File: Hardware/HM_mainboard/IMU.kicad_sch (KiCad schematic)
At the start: 12 parts, among them U5 MC6470, U6 BNO055

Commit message: Updated BOM
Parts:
- C15, C16, C17, C18, C20: Digikey 1276-CL10B104KB8NNNLCT -> 1276-CL10B104KB8NNNLCT-ND
- C19: Mouser 647-F921E105KPA -> F921E105KPA
- R11: value 10k/1% -> 10k; Mouser 660-RN73H1JT1002F100 -> (none)
- U5: Mouser 498-MC6470 -> MC6470
- U6: Mouser 262-BNO055 -> (none)
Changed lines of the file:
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@@
       (effects (font (size 1.27 1.27)) hide)
     )
-    (property "Mouser" "647-F921E105KPA" (at 172.085 77.47 0)
+    (property "Mouser" "F921E105KPA" (at 172.085 77.47 0)
       (effects (font (size 1.27 1.27)) hide)
     )
@@
       (effects (font (size 1.778 1.778)) (justify bottom))
     )
-    (property "Value" "10k/1%" (at 155.575 70.485 0)
+    (property "Value" "10k" (at 155.575 70.485 0)
       (effects (font (size 1.778 1.778)) (justify top))
     )
@@
     )
     (property "Reichelt" "" (at 155.575 64.77 0)
-      (effects (font (size 1.27 1.27)) hide)
-    )
-    (property "Mouser" "660-RN73H1JT1002F100" (at 155.575 64.77 0)
       (effects (font (size 1.27 1.27)) hide)
     )
@@
       (effects (font (size 1.27 1.27)) hide)
     )
-    (property "Digikey" "1276-CL10B104KB8NNNLCT" (at 252.095 52.705 0)
+    (property "Digikey" "1276-CL10B104KB8NNNLCT-ND" (at 252.095 52.705 0)
       (effects (font (size 1.27 1.27)) hide)
     )
@@
       (effects (font (size 1.27 1.27)) hide)
     )
-    (property "Digikey" "1276-CL10B104KB8NNNLCT" (at 56.515 102.235 0)
+    (property "Digikey" "1276-CL10B104KB8NNNLCT-ND" (at 56.515 102.235 0)
       (effects (font (size 1.27 1.27)) hide)
     )
@@
       (effects (font (size 1.27 1.27)) (justify bottom) hide)
     )
-    (property "Mouser" "498-MC6470" (at 60.96 158.115 0)
+    (property "Mouser" "MC6470" (at 60.96 158.115 0)
       (effects (font (size 1.27 1.27)) hide)
     )
@@
       (effects (font (size 1.27 1.27)) hide)
     )
-    (property "Digikey" "1276-CL10B104KB8NNNLCT" (at 86.995 78.105 0)
+    (property "Digikey" "1276-CL10B104KB8NNNLCT-ND" (at 86.995 78.105 0)
       (effects (font (size 1.27 1.27)) hide)
     )
@@
       (effects (font (size 1.27 1.27)) hide)
     )
-    (property "Digikey" "1276-CL10B104KB8NNNLCT" (at 102.87 151.13 0)
+    (property "Digikey" "1276-CL10B104KB8NNNLCT-ND" (at 102.87 151.13 0)
       (effects (font (size 1.27 1.27)) hide)
     )
@@
     )
     (property "Reichelt" "" (at 178.435 57.15 0)
-      (effects (font (size 1.27 1.27)) hide)
-    )
-    (property "Mouser" "262-BNO055" (at 178.435 57.15 0)
       (effects (font (size 1.27 1.27)) hide)
     )
@@
       (effects (font (size 1.778 1.778)) (justify bottom))
     )
-    (property "Value" "10k/1%" (at 87.63 156.21 0)
+    (property "Value" "10k" (at 87.63 156.21 0)
       (effects (font (size 1.778 1.778)) (justify top))
     )
@@
     )
     (property "Reichelt" "" (at 87.63 153.035 0)
-      (effects (font (size 1.27 1.27)) hide)
-    )
-    (property "Mouser" "660-RN73H1JT1002F100" (at 87.63 153.035 0)
       (effects (font (size 1.27 1.27)) hide)
     )
@@
       (effects (font (size 1.27 1.27)) hide)
     )
-    (property "Digikey" "1276-CL10B104KB8NNNLCT" (at 158.115 50.8 0)
+    (property "Digikey" "1276-CL10B104KB8NNNLCT-ND" (at 158.115 50.8 0)
       (effects (font (size 1.27 1.27)) hide)
     )
@@
       (effects (font (size 1.778 1.778)) (justify bottom))
     )
-    (property "Value" "10k/1%" (at 155.575 88.265 0)
+    (property "Value" "10k" (at 155.575 88.265 0)
       (effects (font (size 1.778 1.778)) (justify top))
     )
@@
       (effects (font (size 1.27 1.27)) hide)
     )
-    (property "Mouser" "660-RN73H1JT1002F100" (at 155.575 82.55 0)
-      (effects (font (size 1.27 1.27)) hide)
-    )

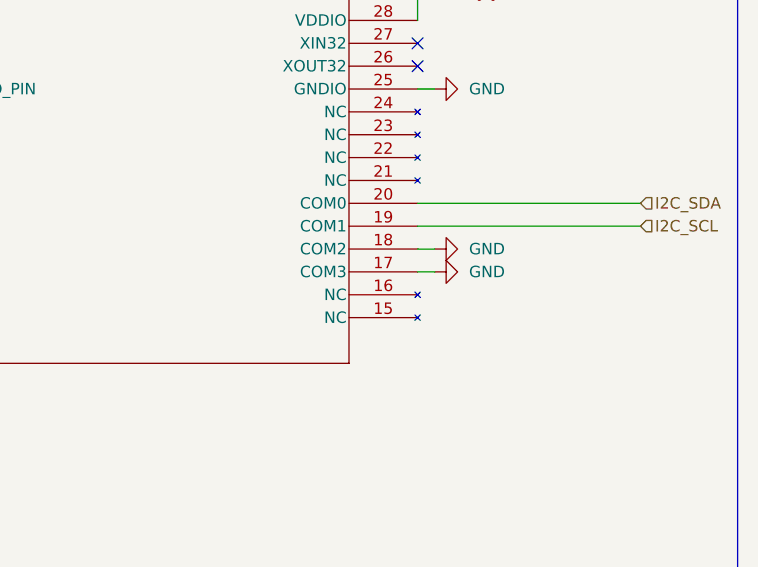
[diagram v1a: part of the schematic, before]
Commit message: Fixed missing GND connections of BNO055 at Pin 15 and 16
Bugfix due to wrong pin assignments in symbol library
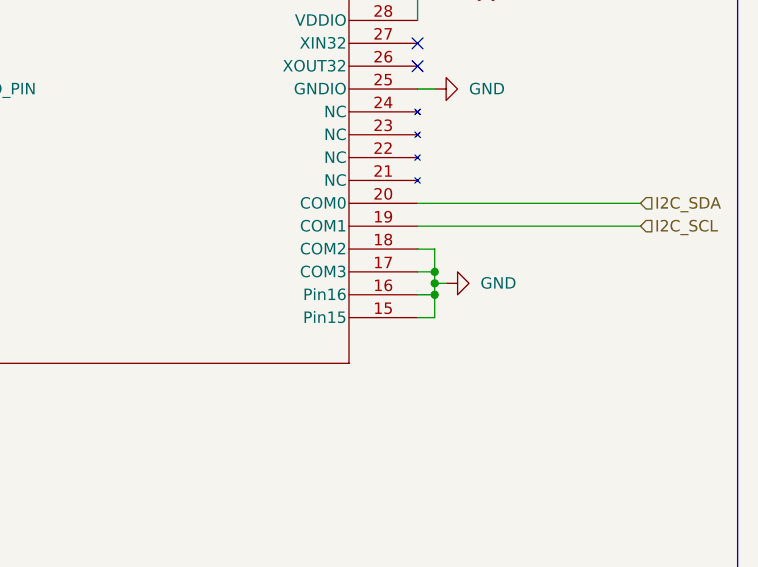
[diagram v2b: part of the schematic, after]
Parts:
- U6: footprint HeadMouse:QFN_BNO055_BOS -> QFN_BNO055_BOS
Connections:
- net GND: now also U6.15 (Pin15), U6.16 (Pin16)
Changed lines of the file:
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@@
   (junction (at 84.455 145.415) (diameter 0) (color 0 0 0 0)
   )
+  (junction (at 246.38 85.09) (diameter 0) (color 0 0 0 0)
+  )
+  (junction (at 246.38 86.36) (diameter 0) (color 0 0 0 0)
+  )
   (junction (at 158.115 45.72) (diameter 0) (color 0 0 0 0)
+  )
+  (junction (at 246.38 87.63) (diameter 0) (color 0 0 0 0)
   )
   (junction (at 86.995 73.025) (diameter 0) (color 0 0 0 0)
@@
     (stroke (width 0) (type default))
   )
+  (wire (pts (xy 244.475 90.17) (xy 246.38 90.17))
+    (stroke (width 0) (type default))
+  )
   (wire (pts (xy 41.275 70.485) (xy 46.355 70.485))
     (stroke (width 0) (type default))
@@
     (stroke (width 0) (type default))
   )
+  (wire (pts (xy 244.475 87.63) (xy 246.38 87.63))
+    (stroke (width 0) (type default))
+  )
   (wire (pts (xy 244.475 82.55) (xy 246.38 82.55))
     (stroke (width 0) (type default))
@@
     (stroke (width 0) (type default))
   )
+  (wire (pts (xy 246.38 87.63) (xy 246.38 86.36))
+    (stroke (width 0) (type default))
+  )
   (wire (pts (xy 175.895 68.58) (xy 177.165 68.58))
     (stroke (width 0) (type default))
@@
     (stroke (width 0) (type default))
   )
+  (wire (pts (xy 246.38 86.36) (xy 246.38 85.09))
+    (stroke (width 0) (type default))
+  )
   (wire (pts (xy 56.515 106.045) (xy 56.515 107.315))
     (stroke (width 0) (type default))
@@
     (stroke (width 0) (type default))
   )
+  (wire (pts (xy 246.38 82.55) (xy 246.38 85.09))
+    (stroke (width 0) (type default))
+  )
   (wire (pts (xy 149.225 64.77) (xy 150.495 64.77))
     (stroke (width 0) (type default))
@@
     (stroke (width 0) (type default))
   )
+  (wire (pts (xy 246.38 90.17) (xy 246.38 87.63))
+    (stroke (width 0) (type default))
+  )
   (wire (pts (xy 86.995 73.025) (xy 86.995 71.755))
     (stroke (width 0) (type default))
@@
   )
   (wire (pts (xy 84.455 145.415) (xy 78.74 145.415))
+    (stroke (width 0) (type default))
+  )
+  (wire (pts (xy 247.65 86.36) (xy 246.38 86.36))
     (stroke (width 0) (type default))
   )
@@
       (effects (font (size 1.524 1.524)))
     )
-    (property "Footprint" "HeadMouse:QFN_BNO055_BOS" (at 178.435 57.15 0)
+    (property "Footprint" "QFN_BNO055_BOS" (at 178.435 57.15 0)
       (effects (font (size 1.27 1.27) italic) hide)
     )
-    (property "Datasheet" "https://www.bosch-sensortec.com/media/boschsensortec/downloads/datasheets/bst-bno055-ds000.pdf" (at 178.435 57.15 0)
+    (property "Datasheet" "BNO055" (at 178.435 57.15 0)
       (effects (font (size 1.27 1.27) italic) hide)
     )
@@
     (pin "13")
     (pin "14")
-    (pin "15")
-    (pin "16")
     (pin "17")
     (pin "18")
@@
     (pin "23")
     (pin "24")
-    (pin "25")
     (pin "26")
     (pin "27")
@@
     (pin "8")
     (pin "9")
+    (pin "15")
+    (pin "16")
+    (pin "25")
     (instances
       (project "HM_mainboard"
@@
     )
   )
-  (symbol (lib_name "GND_1") (lib_id "power:GND") (at 246.38 85.09 90) (unit 1)
-    (in_bom yes) (on_board yes) (dnp no) (fields_autoplaced)
-    (property "Reference" "#PWR06" (at 252.73 85.09 0)
-      (effects (font (size 1.27 1.27)) hide)
-    )
-    (property "Value" "GND" (at 250.19 85.09 90)
+  (symbol (lib_name "GND_1") (lib_id "power:GND") (at 247.65 86.36 90) (unit 1)
+    (in_bom yes) (on_board yes) (dnp no) (fields_autoplaced)
+    (property "Reference" "#PWR06" (at 254 86.36 0)
+      (effects (font (size 1.27 1.27)) hide)
+    )
+    (property "Value" "GND" (at 251.46 86.36 90)
       (effects (font (size 1.27 1.27)) (justify right))
     )
-    (property "Footprint" "" (at 246.38 85.09 0)
-      (effects (font (size 1.27 1.27)) hide)
-    )
-    (property "Datasheet" "" (at 246.38 85.09 0)
+    (property "Footprint" "" (at 247.65 86.36 0)
+      (effects (font (size 1.27 1.27)) hide)
+    )
+    (property "Datasheet" "" (at 247.65 86.36 0)
       (effects (font (size 1.27 1.27)) hide)
     )
@@
         )
       )
-    )
-  )
-  (symbol (lib_name "GND_1") (lib_id "power:GND") (at 246.38 82.55 90) (unit 1)
-    (in_bom yes) (on_board yes) (dnp no) (fields_autoplaced)
-    (property "Reference" "#PWR06" (at 252.73 82.55 0)
-      (effects (font (size 1.27 1.27)) hide)
-    )
-    (property "Value" "GND" (at 250.19 82.55 90)
-      (effects (font (size 1.27 1.27)) (justify right))
-    )
-    (property "Footprint" "" (at 246.38 82.55 0)
-      (effects (font (size 1.27 1.27)) hide)
-    )
-    (property "Datasheet" "" (at 246.38 82.55 0)
-      (effects (font (size 1.27 1.27)) hide)
-    )
-    (pin "1")
-    (instances
-      (project "HM_mainboard"
-        (path "/54a6df43-5475-46a2-9916-8b0260700d4c"
-          (reference "#PWR06") (unit 1)
-        )
-        (path "/54a6df43-5475-46a2-9916-8b0260700d4c/8a725ce3-408a-4762-9df2-b56094186e56"
-          (reference "#PWR09") (unit 1)
-        )
-        (path "/54a6df43-5475-46a2-9916-8b0260700d4c/9043a365-e24a-41b8-9f6d-decb4da0da6a"
-          (reference "#PWR047") (unit 1)
-        )
-      )

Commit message: Added testpoints to pcb
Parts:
- added TP7: TestPoint_2Pole, Connector_PinHeader_2.54mm:PinHeader_1x02_P2.54mm_Vertical, symbol Connector:TestPoint_2Pole
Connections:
- net I2C_SCL: now also TP7.1
- net I2C_SDA: now also TP7.2
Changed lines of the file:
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@@
     (title "Intertia_Measurement_Unit")
   )
+  (junction (at 255.905 80.01) (diameter 0) (color 0 0 0 0)
+  )
   (junction (at 56.515 97.155) (diameter 0) (color 0 0 0 0)
+  )
+  (junction (at 266.065 77.47) (diameter 0) (color 0 0 0 0)
   )
   (junction (at 41.275 67.945) (diameter 0) (color 0 0 0 0)
@@
     (stroke (width 0) (type default))
   )
+  (wire (pts (xy 255.905 74.295) (xy 255.905 80.01))
+    (stroke (width 0) (type default))
+  )
   (wire (pts (xy 177.165 68.58) (xy 177.165 67.31))
     (stroke (width 0) (type default))
@@
     (stroke (width 0) (type default))
   )
+  (wire (pts (xy 266.065 77.47) (xy 269.24 77.47))
+    (stroke (width 0) (type default))
+  )
   (wire (pts (xy 65.405 92.075) (xy 65.405 94.615))
     (stroke (width 0) (type default))
@@
     (stroke (width 0) (type default))
   )
+  (wire (pts (xy 266.065 74.295) (xy 266.065 77.47))
+    (stroke (width 0) (type default))
+  )
   (wire (pts (xy 174.625 90.17) (xy 178.435 90.17))
     (stroke (width 0) (type default))
@@
     (stroke (width 0) (type default))
   )
+  (wire (pts (xy 255.905 80.01) (xy 269.24 80.01))
+    (stroke (width 0) (type default))
+  )
   (wire (pts (xy 84.455 145.415) (xy 78.74 145.415))
     (stroke (width 0) (type default))
@@
     (stroke (width 0) (type default))
   )
-  (wire (pts (xy 244.475 80.01) (xy 269.24 80.01))
+  (wire (pts (xy 244.475 80.01) (xy 255.905 80.01))
     (stroke (width 0) (type default))
   )
@@
     (stroke (width 0) (type default))
   )
-  (wire (pts (xy 244.475 77.47) (xy 269.24 77.47))
+  (wire (pts (xy 244.475 77.47) (xy 266.065 77.47))
     (stroke (width 0) (type default))
   )
@@
         )
         (path "/54a6df43-5475-46a2-9916-8b0260700d4c/9043a365-e24a-41b8-9f6d-decb4da0da6a"
-          (reference "#PWR049") (unit 1)
+          (reference "#PWR048") (unit 1)
         )
       )
@@
     )
   )
+  (symbol (lib_id "Connector:TestPoint_2Pole") (at 260.985 74.295 0) (unit 1)
+    (in_bom yes) (on_board yes) (dnp no) (fields_autoplaced)
+    (property "Reference" "TP7" (at 260.985 71.12 0)
+      (effects (font (size 1.27 1.27)))
+    )
+    (property "Value" "TestPoint_2Pole" (at 260.985 71.12 0)
+      (effects (font (size 1.27 1.27)) hide)
+    )
+    (property "Footprint" "Connector_PinHeader_2.54mm:PinHeader_1x02_P2.54mm_Vertical" (at 260.985 74.295 0)
+      (effects (font (size 1.27 1.27)) hide)
+    )
+    (property "Datasheet" "~" (at 260.985 74.295 0)
+      (effects (font (size 1.27 1.27)) hide)
+    )
+    (pin "1")
+    (pin "2")
+    (instances
+      (project "HM_mainboard"
+        (path "/54a6df43-5475-46a2-9916-8b0260700d4c/9043a365-e24a-41b8-9f6d-decb4da0da6a"
+          (reference "TP7") (unit 1)
+        )
+      )
+    )
+  )
   (symbol (lib_name "GND_1") (lib_id "power:GND") (at 65.405 94.615 0) (unit 1)
     (in_bom yes) (on_board yes) (dnp no) (fields_autoplaced)
@@
         )
         (path "/54a6df43-5475-46a2-9916-8b0260700d4c/9043a365-e24a-41b8-9f6d-decb4da0da6a"
-          (reference "#PWR048") (unit 1)
-        )
-      )
+          (reference "#PWR047") (unit 1)
+        )
+      )

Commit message: Updated schematic and PCB according to Email from BA on 16th of April
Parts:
- C19: value 1.0uF-25V-(+80/-20%) -> 1.0uF
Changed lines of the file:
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@@
-    (stroke (width 0) (type default))
-  )
-  (wire (pts (xy 78.74 155.575) (xy 78.74 158.115))
     (stroke (width 0) (type default))
   )
@@
     (stroke (width 0) (type default))
   )
-  (wire (pts (xy 81.915 158.115) (xy 78.74 158.115))
+  (wire (pts (xy 82.55 155.575) (xy 78.74 155.575))
     (stroke (width 0) (type default))
   )
@@
     (stroke (width 0) (type default))
   )
-  (rectangle (start 133.985 16.51) (end 280.035 139.7)
+  (rectangle (start 133.985 16.51) (end 280.035 114.3)
     (stroke (width 0) (type default))
     (fill (type none))
@@
     (effects (font (size 1.27 1.27)) (justify right))
   )
-  (hierarchical_label "MC6470_INT" (shape input) (at 81.915 158.115 0) (fields_autoplaced)
+  (hierarchical_label "MC6470_INT" (shape input) (at 82.55 155.575 0) (fields_autoplaced)
     (effects (font (size 1.27 1.27)) (justify left))
   )
@@
       (effects (font (size 1.27 1.27)))
     )
-    (property "Value" "1.0uF-25V-(+80/-20%)" (at 172.085 73.66 90)
+    (property "Value" "1.0uF" (at 172.085 73.66 90)
       (effects (font (size 1.27 1.27)))
     )
@@
   (symbol (lib_id "esp32-thing-eagle-import:10KOHM-1/10W-1%(0603)0603") (at 87.63 153.035 180) (unit 1)
     (in_bom yes) (on_board yes) (dnp no)
-    (property "Reference" "R11" (at 87.63 149.86 0)
+    (property "Reference" "R11" (at 87.63 147.32 0)
       (effects (font (size 1.778 1.778)) (justify bottom))
     )
-    (property "Value" "10k" (at 87.63 156.21 0)
+    (property "Value" "10k" (at 87.63 151.765 0)
       (effects (font (size 1.778 1.778)) (justify top))
     )
@@
   )
   (symbol (lib_name "GND_1") (lib_id "power:GND") (at 65.405 94.615 0) (unit 1)
-    (in_bom yes) (on_board yes) (dnp no) (fields_autoplaced)
+    (in_bom yes) (on_board yes) (dnp no)
     (property "Reference" "#PWR06" (at 65.405 100.965 0)
       (effects (font (size 1.27 1.27)) hide)
     )
-    (property "Value" "GND" (at 65.405 99.695 0)
+    (property "Value" "GND" (at 65.405 98.425 0)
       (effects (font (size 1.27 1.27)))
     )
